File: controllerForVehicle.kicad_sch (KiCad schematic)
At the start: 0 parts

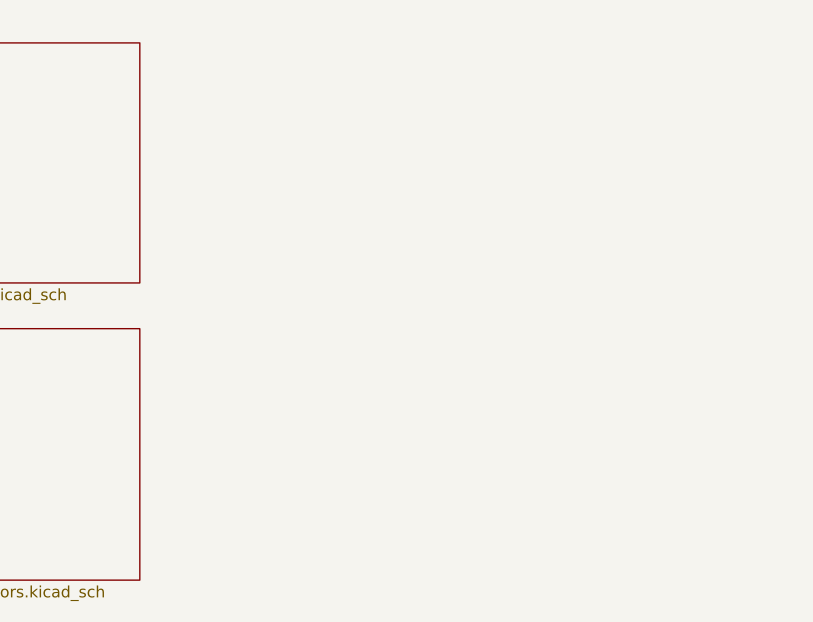
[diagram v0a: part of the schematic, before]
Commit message: added components
servo controller, esp32
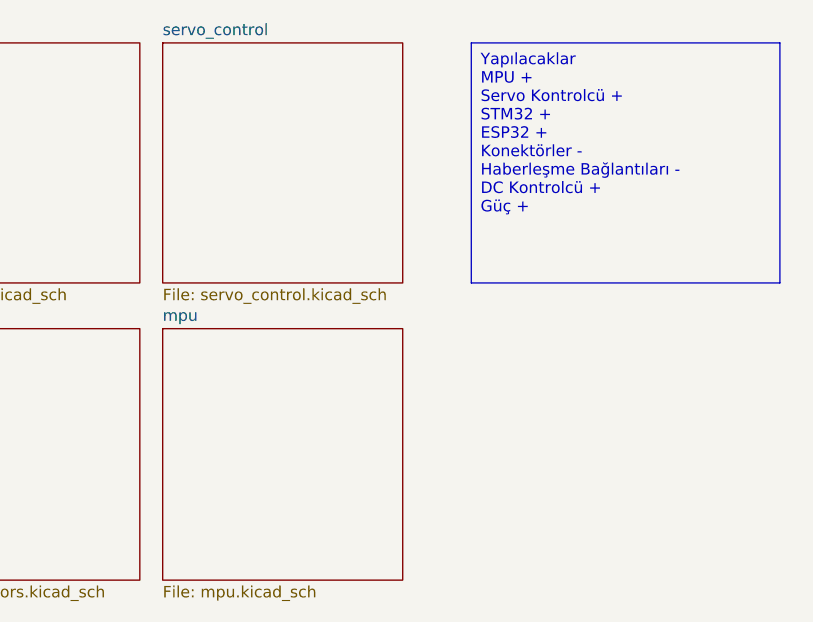
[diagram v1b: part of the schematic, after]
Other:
- added sheet mpu (mpu.kicad_sch)
- added sheet servo_control (servo_control.kicad_sch)
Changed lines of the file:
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@@
 	(generator_version "8.0")
 	(paper "A4")
+	(text_box "Yapılacaklar\nMPU +\nServo Kontrolcü +\nSTM32 +\nESP32 +\nKonektörler -\nHaberleşme Bağlantıları -\nDC Kontrolcü + \nGüç +\n"
+		(exclude_from_sim no)
+		(at 133.35 15.24 0)
+		(size 34.29 26.67)
+		(stroke
+			(width 0)
+			(type default)
+		)
+		(fill
+			(type none)
+		)
+		(effects
+			(font
+				(size 1.27 1.27)
+			)
+			(justify left top)
+		)
+	)
+	(text "\n\n\n\n"
+		(exclude_from_sim no)
+		(at 162.814 61.214 0)
+		(effects
+			(font
+				(size 1.27 1.27)
+			)
+		)
+	)
 	(sheet
 		(at 13.97 46.99)
@@
 	)
 	(sheet
+		(at 99.06 15.24)
+		(size 26.67 26.67)
+		(fields_autoplaced yes)
+		(stroke
+			(width 0.1524)
+			(type solid)
+		)
+		(fill
+			(color 0 0 0 0.0000)
+		)
+		(property "Sheetname" "servo_control"
+			(at 99.06 14.5284 0)
+			(effects
+				(font
+					(size 1.27 1.27)
+				)
+				(justify left bottom)
+			)
+		)
+		(property "Sheetfile" "servo_control.kicad_sch"
+			(at 99.06 42.4946 0)
+			(effects
+				(font
+					(size 1.27 1.27)
+				)
+				(justify left top)
+			)
+		)
+		(instances
+			(project "controllerForVehicle"
+				(path "/f177fb06-71dc-4865-9331-a828b12c2bf7"
+					(page "8")
+				)
+			)
+		)
+	)
+	(sheet
 		(at 13.97 15.24)
 		(size 27.94 26.67)
@@
 				)
 			)
+		)
+	)
+	(sheet
+		(at 99.06 46.99)
+		(size 26.67 27.94)
+		(fields_autoplaced yes)
+		(stroke
+			(width 0.1524)
+			(type solid)
+		)
+		(fill
+			(color 0 0 0 0.0000)
+		)
+		(property "Sheetname" "mpu"
+			(at 99.06 46.2784 0)
+			(effects
+				(font
+					(size 1.27 1.27)
+				)
+				(justify left bottom)
+			)
+		)
+		(property "Sheetfile" "mpu.kicad_sch"
+			(at 99.06 75.5146 0)
+			(effects
+				(font
+					(size 1.27 1.27)
+				)
+				(justify left top)
+			)
+		)
+		(instances
+			(project "controllerForVehicle"
+				(path "/f177fb06-71dc-4865-9331-a828b12c2bf7"
+					(page "9")
+				)
+			)

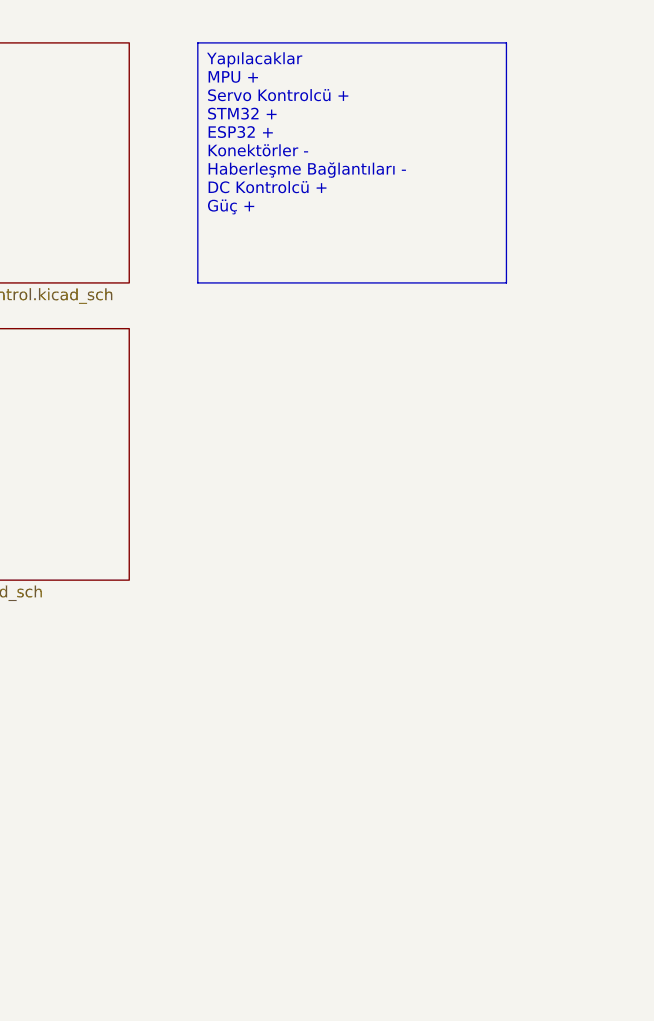
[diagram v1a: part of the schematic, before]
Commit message: gpio expander added comm finished
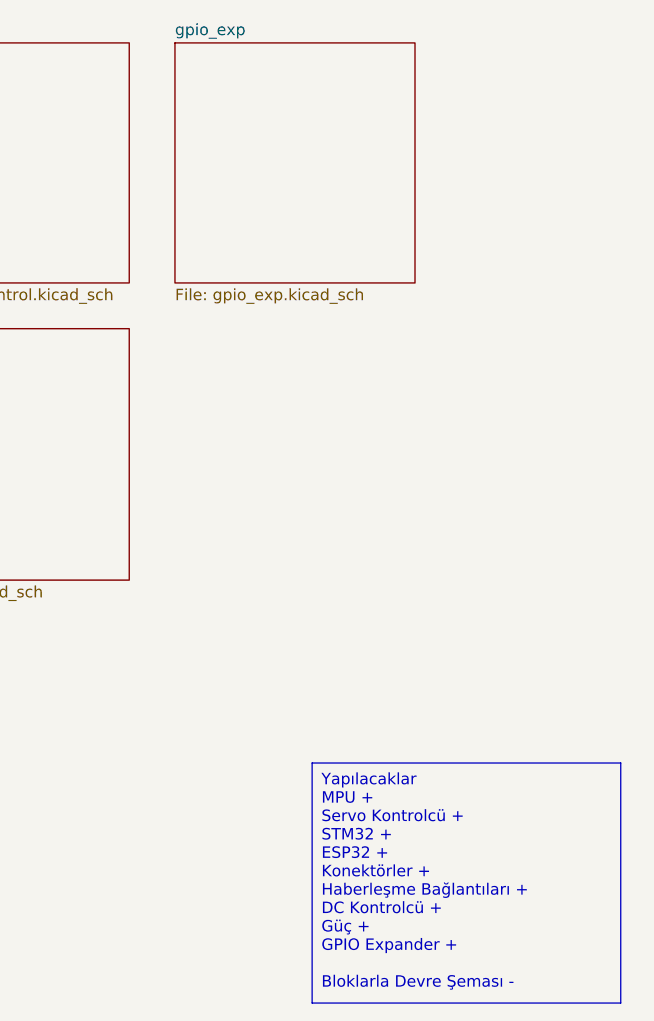
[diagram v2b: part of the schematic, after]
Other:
- added sheet gpio_exp (gpio_exp.kicad_sch)
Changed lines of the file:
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@@
 	(generator_version "8.0")
 	(paper "A4")
-	(text_box "Yapılacaklar\nMPU +\nServo Kontrolcü +\nSTM32 +\nESP32 +\nKonektörler -\nHaberleşme Bağlantıları -\nDC Kontrolcü + \nGüç +\n"
+	(text_box "Yapılacaklar\nMPU +\nServo Kontrolcü +\nSTM32 +\nESP32 +\nKonektörler +\nHaberleşme Bağlantıları +\nDC Kontrolcü + \nGüç +\nGPIO Expander + \n\nBloklarla Devre Şeması -\n"
 		(exclude_from_sim no)
-		(at 133.35 15.24 0)
+		(at 146.05 95.25 0)
 		(size 34.29 26.67)
 		(stroke
@@
 				)
 			)
+		)
+	)
+	(sheet
+		(at 130.81 15.24)
+		(size 26.67 26.67)
+		(fields_autoplaced yes)
+		(stroke
+			(width 0.1524)
+			(type solid)
+		)
+		(fill
+			(color 0 0 0 0.0000)
+		)
+		(property "Sheetname" "gpio_exp"
+			(at 130.81 14.5284 0)
+			(effects
+				(font
+					(size 1.27 1.27)
+				)
+				(justify left bottom)
+			)
+		)
+		(property "Sheetfile" "gpio_exp.kicad_sch"
+			(at 130.81 42.4946 0)
+			(effects
+				(font
+					(size 1.27 1.27)
+				)
+				(justify left top)
+			)
+		)
+		(instances
+			(project "controllerForVehicle"
+				(path "/f177fb06-71dc-4865-9331-a828b12c2bf7"
+					(page "10")
+				)
+			)

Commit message: Routing
Routing STM32 and Components
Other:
- note added: "1. katman sinyal 2. gnd 3. power 4. sinyal"
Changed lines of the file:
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@@
+		)
+	)
+	(text "1. katman sinyal\n2. gnd\n3. power\n4. sinyal"
+		(exclude_from_sim no)
+		(at 147.574 131.064 0)
+		(effects
+			(font
+				(size 1.27 1.27)
+			)
+			(justify left)
 		)
 	)

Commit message: esp32 silindi, yerleştirmeler yapıldı
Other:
- removed sheet mcu_esp32
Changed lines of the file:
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@@
 	(text "\n\n\n\n"
 		(exclude_from_sim no)
-		(at 162.814 61.214 0)
+		(at 162.56 60.96 0)
 		(effects
 			(font
@@
 		)
 	)
-	(sheet
-		(at 13.97 46.99)
-		(size 27.94 27.94)
-		(fields_autoplaced yes)
-		(stroke
-			(width 0.1524)
-			(type solid)
-		)
-		(fill
-			(color 0 0 0 0.0000)
-		)
-		(property "Sheetname" "mcu_esp32"
-			(at 13.97 46.2784 0)
-			(effects
-				(font
-					(size 1.27 1.27)
-				)
-				(justify left bottom)
-			)
-		)
-		(property "Sheetfile" "mcu_esp32.kicad_sch"
-			(at 13.97 75.5146 0)
-			(effects
-				(font
-					(size 1.27 1.27)
-				)
-				(justify left top)
-			)
-		)
-		(instances
-			(project "controllerForVehicle"
-				(path "/f177fb06-71dc-4865-9331-a828b12c2bf7"
-					(page "4")
-				)
-			)
-		)
-	)
